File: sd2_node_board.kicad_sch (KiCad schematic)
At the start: 21 parts

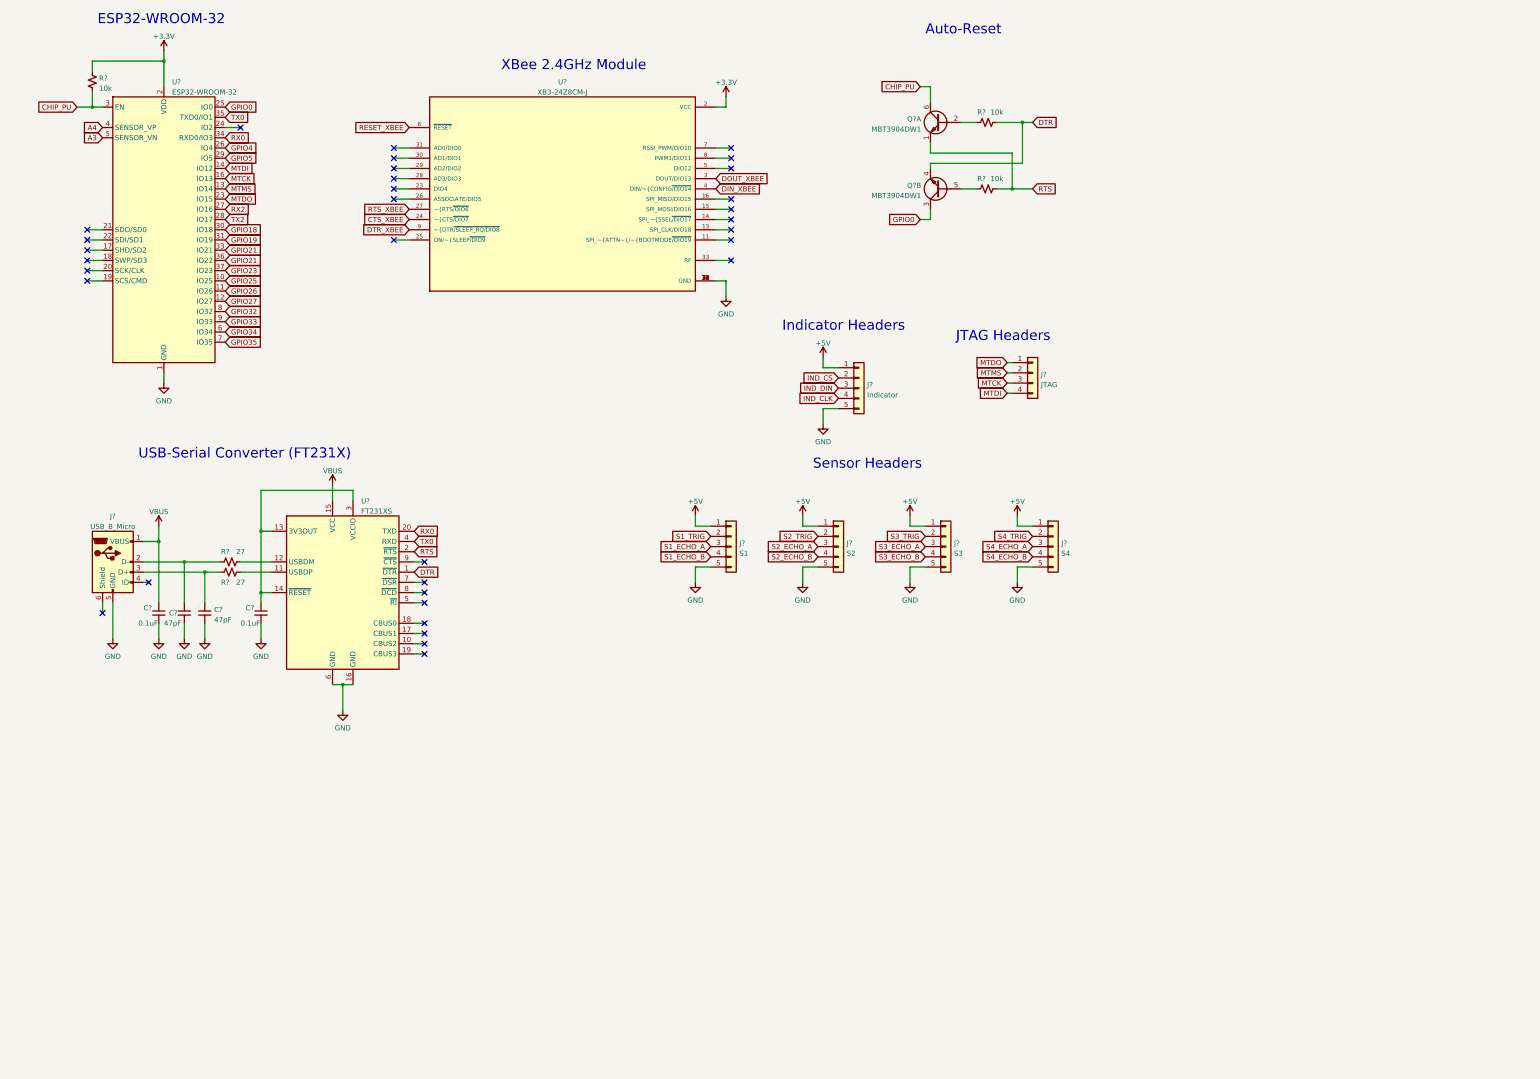
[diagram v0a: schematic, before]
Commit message: Add components to schematic
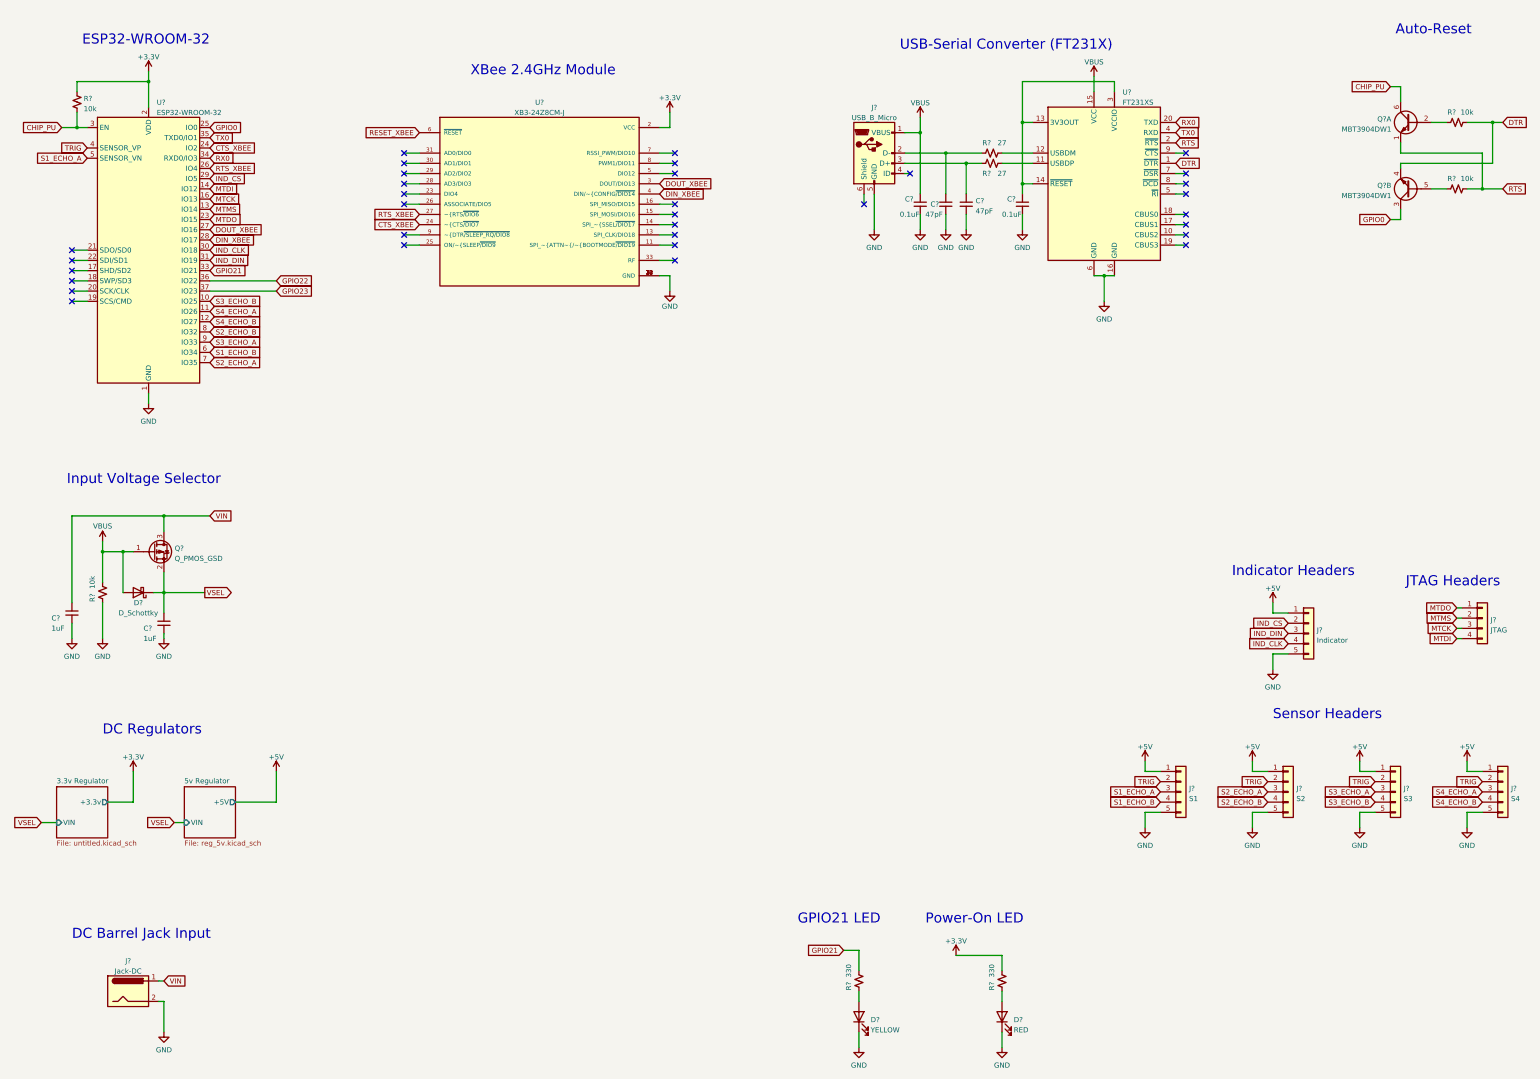
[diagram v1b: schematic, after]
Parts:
- removed U?: XB3-24Z8CM-J, XBee:XB3-24Z8UM-J, symbol XBee:XB3-24Z8CM-J
- added C? (x2): 1uF, Capacitor_SMD:C_0805_2012Metric_Pad1.18x1.45mm_HandSolder, symbol Device:C_Small
- added D?: YELLOW, symbol Device:LED
- added D?: RED, symbol Device:LED
- added D?: D_Schottky, Diode_SMD:D_SOD-123, symbol Device:D_Schottky
- added J?: Jack-DC, symbol Connector:Jack-DC
- added Q?: Q_PMOS_GSD, Package_TO_SOT_SMD:SOT-23, symbol Device:Q_PMOS_GSD
- added R? (x2): 330, Resistor_SMD:R_0805_2012Metric_Pad1.20x1.40mm_HandSolder, symbol Device:R_Small_US
- added R?: 10k, Resistor_SMD:R_0805_2012Metric_Pad1.20x1.40mm_HandSolder, symbol Device:R_Small_US
- added U?: XB3-24Z8CM-J, XCVR_XB3-24Z8CM-J, symbol XBee:XB3-24Z8CM-J
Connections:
- net A3 is gone; now on net S1_ECHO_A: U?.5 (SENSOR_VN)
- net GPIO18 is gone; now on net IND_CLK: U?.30 (IO18)
- net GPIO19 is gone; now on net IND_DIN: U?.31 (IO19)
- net GPIO25 is gone; now on net S3_ECHO_B: U?.10 (IO25)
- net GPIO26 is gone; now on net S4_ECHO_A: U?.11 (IO26)
- net GPIO27 is gone; now on net S4_ECHO_B: U?.12 (IO27)
- net GPIO32 is gone; now on net S2_ECHO_B: U?.8 (IO32)
- net GPIO33 is gone; now on net S3_ECHO_A: U?.9 (IO33)
- net GPIO34 is gone; now on net S1_ECHO_B: U?.6 (IO34)
- net GPIO35 is gone; now on net S2_ECHO_A: U?.7 (IO35)
- net GPIO4 is gone; now on net RTS_XBEE: U?.26 (IO4)
- net GPIO5 is gone; now on net IND_CS: U?.29 (IO5)
- net RX2 is gone; now on net DOUT_XBEE: U?.27 (IO16)
- net S1_TRIG is gone; now on net TRIG: J?.2 (Pin_2)
- net S2_TRIG is gone; now on net TRIG: J?.2 (Pin_2)
- net S3_TRIG is gone; now on net TRIG: J?.2 (Pin_2)
- net S4_TRIG is gone; now on net TRIG: J?.2 (Pin_2)
- net TX2 is gone; now on net DIN_XBEE: U?.28 (IO17)
- net +3.3V: now also R?.1, U?.2 (VCC)
- net CTS_XBEE: now also U?.24 (IO2), U?.24 (~{CTS~{/DIO7})
- net DIN_XBEE: now also U?.4 (DIN/~{CONFIG~{/DIO14})
- net DOUT_XBEE: now also U?.3 (DOUT/DIO13)
- net GND: now also C?.2, C?.2, D?.1 (K), D?.1 (K), J?.2, R?.2, U?.1 (GND), U?.10 (GND), U?.12 (GND), U?.21 (GND), U?.32 (GND), U?.34 (GND)
- net GPIO21: now also R?.1; no longer U?.36 (IO22)
- net RESET_XBEE: now also U?.6 (~{RESET})
- net RTS_XBEE: now also U?.27 (~{RTS~{/DIO6})
- net VBUS: now also D?.2 (A), Q?.1 (G), R?.1
- net A4 renamed TRIG
- new net: D?.2 (A), R?.2 (x2)
- new net GPIO22: U?.36 (IO22)
- new net VIN: C?.1, J?.1, Q?.3 (D)
- new net VSEL: C?.1, D?.1 (K), Q?.2 (S)
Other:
- added sheet 3.3v Regulator (untitled.kicad_sch)
- added sheet 5v Regulator (reg_5v.kicad_sch)
- note added: "DC Barrel Jack Input"
- note added: "DC Regulators"
- note added: "GPIO21 LED"
- note added: "Input Voltage Selector"
- note added: "Power-On LED"
- moved on the sheet: C?, J?, Q?A, Q?B, R?, U?

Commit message: Finish schematic and start routing PCB
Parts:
- removed C? (x2): 1uF, Capacitor_SMD:C_0805_2012Metric_Pad1.18x1.45mm_HandSolder, symbol Device:C_Small
- removed D?: D_Schottky, Diode_SMD:D_SOD-123, symbol Device:D_Schottky
- removed J?: Jack-DC, symbol Connector:Jack-DC
- removed Q?: Q_PMOS_GSD, Package_TO_SOT_SMD:SOT-23, symbol Device:Q_PMOS_GSD
- removed R?: 10k, Resistor_SMD:R_0805_2012Metric_Pad1.20x1.40mm_HandSolder, symbol Device:R_Small_US
- added J1: CON-SOCJ-2155, Connector:GRAVITECH_CON-SOCJ-2155, symbol Connector:CON-SOCJ-2155
- added SW1: SW_Push, Button_Switch_SMD:SW_Tactile_SPST_NO_Straight_CK_PTS636Sx25SMTRLFS, symbol Switch:SW_Push
- D1, D2: renamed from D?; footprint (none) -> LED_SMD:LED_0805_2012Metric_Pad1.15x1.40mm_HandSolder
- J3, J4, J5, J6, J8: renamed from J?; footprint (none) -> TerminalBlock_Phoenix:TerminalBlock_Phoenix_MKDS-1,5-5-5.08_1x05_P5.08mm_Horizontal
- J7: renamed from J?; footprint (none) -> Connector_PinHeader_2.54mm:PinHeader_1x04_P2.54mm_Vertical
- U2: renamed from U?; footprint XCVR_XB3-24Z8CM-J -> XBee:XB3-24Z8UM-J
- gave numbers to parts that had none: 15
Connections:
- net CHIP_PU: now also SW1.2
- net GND: now also J1.3, SW1.1
- net GPIO0: now also J6.2 (Pin_2)
- net IND_CLK: now also J5.3 (Pin_3); no longer J5.4 (Pin_4)
- net IND_CS: now also J5.4 (Pin_4); no longer J5.2 (Pin_2)
- net IND_DIN: now also J5.2 (Pin_2); no longer J5.3 (Pin_3)
- net MTDI: now also J7.2 (Pin_2); no longer J7.4 (Pin_4)
- net MTDO: now also J7.4 (Pin_4); no longer J7.1 (Pin_1)
- net MTMS: now also J7.1 (Pin_1); no longer J7.2 (Pin_2)
- net VIN: now also J1.1
- net GPIO22 renamed TRIG2
- net TRIG2: now also J4.2 (Pin_2)
- net GPIO23 renamed TRIG4
- net TRIG4: now also J8.2 (Pin_2)
- net RESET_XBEE: no longer names the net of U2.6 (~{RESET})
- removed net TRIG: J3.2 (Pin_2), J4.2 (Pin_2), J6.2 (Pin_2), J8.2 (Pin_2), U1.4 (SENSOR_VP)
- new net TRIG1: J3.2 (Pin_2), U1.4 (SENSOR_VP)
- no-connect marks 33 -> 35
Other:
- sheet 3.3v Regulator: file untitled.kicad_sch -> reg_3v3.kicad_sch
- note added: "Reset Button"
- note removed: "Input Voltage Selector"
